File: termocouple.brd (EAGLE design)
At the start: 69.8 x 100 mm, 19 parts, among them IC1 MAX6675, IC2 MAX6675, U2 TC1262_VDB, X2 1751248, X3 1751248

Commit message: updated brd
finished routing PCB
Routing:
- net N$12: track 0.00 -> 94.5 mm, vias 0 -> 1
- net N$11: track 0.00 -> 88.4 mm, vias 0 -> 1
- net N$9: track 0.00 -> 73.2 mm, vias 0 -> 1
- net N$23: track 0.00 -> 65.2 mm, vias 0 -> 1
- net N$22: track 0.00 -> 64.0 mm, vias 0 -> 1
- net +3V3: track 194.9 -> 181.8 mm
- net VJ: track 6.70 -> 8.97 mm
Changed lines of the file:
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@@
 <wire x1="10.29" y1="41.91" x2="10.29" y2="44.32" width="0.8128" layer="1"/>
 <wire x1="10.29" y1="44.32" x2="8.89" y2="45.72" width="0.8128" layer="1"/>
-<wire x1="8.89" y1="45.72" x2="6.985" y2="45.72" width="0.8128" layer="1"/>
-<wire x1="6.985" y1="45.72" x2="5.08" y2="45.72" width="0.8128" layer="1"/>
+<wire x1="8.89" y1="45.72" x2="5.08" y2="45.72" width="0.8128" layer="1"/>
 <wire x1="5.08" y1="45.72" x2="3.81" y2="46.99" width="0.8128" layer="1"/>
-<wire x1="3.81" y1="46.99" x2="3.81" y2="80.01" width="0.8128" layer="1"/>
+<wire x1="3.81" y1="46.99" x2="3.81" y2="60.96" width="0.8128" layer="1"/>
+<wire x1="3.81" y1="60.96" x2="3.81" y2="80.01" width="0.8128" layer="1"/>
 <wire x1="3.81" y1="80.01" x2="11.43" y2="87.63" width="0.8128" layer="1"/>
 <wire x1="11.43" y1="87.63" x2="20.32" y2="87.63" width="0.8128" layer="1"/>
-<wire x1="55.88" y1="60.96" x2="8.255" y2="60.96" width="0.6096" layer="16"/>
-<wire x1="8.255" y1="60.96" x2="6.985" y2="59.69" width="0.6096" layer="16"/>
-<wire x1="6.985" y1="59.69" x2="6.985" y2="45.72" width="0.6096" layer="16"/>
-<via x="6.985" y="45.72" extent="1-16" drill="0.6" shape="square"/>
+<wire x1="54.61" y1="60.96" x2="8.255" y2="60.96" width="0.6096" layer="16"/>
 <wire x1="60.325" y1="31.2166" x2="60.325" y2="34.29" width="0.6096" layer="1"/>
 <wire x1="60.325" y1="34.29" x2="43.815" y2="34.29" width="0.6096" layer="1"/>
@@
 <wire x1="64.77" y1="34.29" x2="60.325" y2="34.29" width="0.4064" layer="16"/>
 <via x="60.325" y="34.29" extent="1-16" drill="0.6" shape="square"/>
-<wire x1="55.88" y1="60.96" x2="55.88" y2="57.785" width="0.4064" layer="16"/>
-<wire x1="55.88" y1="57.785" x2="54.61" y2="56.515" width="0.4064" layer="16"/>
-<wire x1="54.61" y1="56.515" x2="54.61" y2="48.26" width="0.4064" layer="16"/>
+<wire x1="54.61" y1="60.96" x2="54.61" y2="48.26" width="0.6096" layer="16"/>
+<via x="8.255" y="60.96" extent="1-16" drill="0.6" shape="square"/>
+<wire x1="8.255" y1="60.96" x2="3.81" y2="60.96" width="0.6096" layer="1"/>
 </signal>
 <signal name="GND">
@@
 <contactref element="SV1" pad="2"/>
 <contactref element="SV1" pad="6"/>
+<via x="22.86" y="8.255" extent="1-16" drill="0.6" shape="square"/>
+<via x="32.385" y="57.15" extent="1-16" drill="0.6" shape="square"/>
+<via x="26.67" y="68.58" extent="1-16" drill="0.6" shape="square"/>
+<via x="32.385" y="69.215" extent="1-16" drill="0.6" shape="square"/>
+<via x="32.385" y="79.375" extent="1-16" drill="0.6" shape="square"/>
+<via x="26.67" y="78.105" extent="1-16" drill="0.6" shape="square"/>
+<via x="65.405" y="51.435" extent="1-16" drill="0.6" shape="square"/>
+<via x="39.37" y="48.26" extent="1-16" drill="0.6" shape="square"/>
+<via x="39.37" y="48.26" extent="1-16" drill="0.6" shape="square"/>
+<via x="20.955" y="41.91" extent="1-16" drill="0.6" shape="square"/>
+<via x="6.985" y="56.515" extent="1-16" drill="0.6" shape="square"/>
 </signal>
 <signal name="N$4">
@@
 <wire x1="5.89289375" y1="13.77779375" x2="5.42" y2="14.41279375" width="0.8128" layer="1"/>
 <wire x1="5.42" y1="14.41279375" x2="5.42" y2="20.32" width="0.8128" layer="1"/>
-<wire x1="5.89289375" y1="13.77779375" x2="8.09625" y2="13.795" width="0" layer="19" extent="1-1"/>
+<wire x1="6.35" y1="13.97" x2="7.62" y2="13.97" width="0.254" layer="1"/>
+<wire x1="7.62" y1="13.97" x2="8.09625" y2="13.795" width="0.254" layer="1"/>
+<wire x1="6.35" y1="13.97" x2="5.89289375" y2="13.77779375" width="0.254" layer="1"/>
 </signal>
 <signal name="N$18">
@@
 <contactref element="U$1" pad="D6"/>
 <contactref element="X1" pad="5"/>
-<wire x1="30.48" y1="19.05" x2="30.48" y2="87.63" width="0" layer="19" extent="1-1"/>
+<wire x1="30.48" y1="19.05" x2="27.94" y2="19.05" width="0.4064" layer="16"/>
+<wire x1="27.94" y1="19.05" x2="26.67" y2="20.32" width="0.4064" layer="16"/>
+<wire x1="26.67" y1="20.32" x2="26.67" y2="40.005" width="0.4064" layer="16"/>
+<wire x1="26.67" y1="40.005" x2="29.21" y2="42.545" width="0.4064" layer="16"/>
+<wire x1="29.21" y1="42.545" x2="29.21" y2="58.42" width="0.4064" layer="16"/>
+<via x="29.21" y="58.42" extent="1-16" drill="0.6" shape="square"/>
+<wire x1="29.21" y1="58.42" x2="29.21" y2="81.915" width="0.4064" layer="1"/>
+<wire x1="29.21" y1="81.915" x2="30.48" y2="83.185" width="0.4064" layer="1"/>
+<wire x1="30.48" y1="83.185" x2="30.48" y2="87.63" width="0.4064" layer="1"/>
 </signal>
 <signal name="N$10">
@@
 <contactref element="U$1" pad="D4"/>
 <contactref element="X1" pad="7"/>
-<wire x1="30.48" y1="13.97" x2="35.56" y2="87.63" width="0" layer="19" extent="1-1"/>
+<wire x1="30.48" y1="13.97" x2="25.4" y2="13.97" width="0.4064" layer="16"/>
+<wire x1="25.4" y1="13.97" x2="24.13" y2="15.24" width="0.4064" layer="16"/>
+<wire x1="24.13" y1="15.24" x2="24.13" y2="39.37" width="0.4064" layer="16"/>
+<wire x1="24.13" y1="39.37" x2="27.94" y2="43.18" width="0.4064" layer="16"/>
+<wire x1="27.94" y1="43.18" x2="27.94" y2="52.07" width="0.4064" layer="16"/>
+<wire x1="27.94" y1="52.07" x2="26.67" y2="53.34" width="0.4064" layer="16"/>
+<via x="26.67" y="53.34" extent="1-16" drill="0.6" shape="square"/>
+<wire x1="26.67" y1="53.34" x2="32.385" y2="53.34" width="0.4064" layer="1"/>
+<wire x1="32.385" y1="53.34" x2="35.56" y2="56.515" width="0.4064" layer="1"/>
+<wire x1="35.56" y1="56.515" x2="35.56" y2="87.63" width="0.4064" layer="1"/>
 </signal>
 <signal name="N$12">
 <contactref element="U$1" pad="D3"/>
 <contactref element="X1" pad="8"/>
-<wire x1="30.48" y1="11.43" x2="38.1" y2="87.63" width="0" layer="19" extent="1-1"/>
+<wire x1="30.48" y1="11.43" x2="22.86" y2="11.43" width="0.4064" layer="16"/>
+<wire x1="22.86" y1="11.43" x2="22.225" y2="12.065" width="0.4064" layer="16"/>
+<wire x1="22.225" y1="12.065" x2="22.225" y2="39.37" width="0.4064" layer="16"/>
+<wire x1="22.225" y1="39.37" x2="26.67" y2="43.815" width="0.4064" layer="16"/>
+<wire x1="26.67" y1="43.815" x2="26.67" y2="48.26" width="0.4064" layer="16"/>
+<wire x1="26.67" y1="48.26" x2="26.035" y2="48.895" width="0.4064" layer="16"/>
+<via x="26.035" y="48.895" extent="1-16" drill="0.6" shape="square"/>
+<wire x1="26.035" y1="48.895" x2="31.75" y2="48.895" width="0.4064" layer="1"/>
+<wire x1="31.75" y1="48.895" x2="38.1" y2="55.245" width="0.4064" layer="1"/>
+<wire x1="38.1" y1="55.245" x2="38.1" y2="87.63" width="0.4064" layer="1"/>
 </signal>
 <signal name="N$22">
 <contactref element="U$1" pad="D0"/>
 <contactref element="X6" pad="3"/>
-<wire x1="15.24" y1="11.43" x2="15.875" y2="67.945" width="0" layer="19" extent="1-1"/>
+<wire x1="15.24" y1="11.43" x2="17.78" y2="11.43" width="0.4064" layer="16"/>
+<wire x1="17.78" y1="11.43" x2="17.78" y2="53.34" width="0.4064" layer="16"/>
+<via x="17.78" y="53.34" extent="1-16" drill="0.6" shape="square"/>
+<wire x1="17.78" y1="53.34" x2="20.32" y2="53.34" width="0.4064" layer="1"/>
+<wire x1="20.32" y1="53.34" x2="20.955" y2="53.975" width="0.4064" layer="1"/>
+<wire x1="20.955" y1="53.975" x2="20.955" y2="62.865" width="0.4064" layer="1"/>
+<wire x1="20.955" y1="62.865" x2="15.875" y2="67.945" width="0.4064" layer="1"/>
 </signal>
 <signal name="N$23">
 <contactref element="U$1" pad="D1"/>
 <contactref element="X6" pad="2"/>
-<wire x1="15.24" y1="8.89" x2="13.335" y2="67.945" width="0" layer="19" extent="1-1"/>
+<wire x1="15.24" y1="8.89" x2="19.05" y2="8.89" width="0.4064" layer="16"/>
+<wire x1="19.05" y1="8.89" x2="19.05" y2="57.785" width="0.4064" layer="16"/>
+<via x="19.05" y="57.785" extent="1-16" drill="0.6" shape="square"/>
+<wire x1="19.05" y1="57.785" x2="19.05" y2="58.42" width="0.4064" layer="1"/>
+<wire x1="19.05" y1="58.42" x2="13.335" y2="64.135" width="0.4064" layer="1"/>
+<wire x1="13.335" y1="64.135" x2="13.335" y2="67.945" width="0.4064" layer="1"/>
 </signal>
 <signal name="N$7">

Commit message: pdf version of schematics
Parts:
- IC1, IC2: value MAX6675 -> MAX31855
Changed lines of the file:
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@@
 <elements>
 <element name="U$1" library="mine" package="EMPHYREAN" value="EPHYREAN" x="22.86" y="26.67"/>
-<element name="IC1" library="adafruit" package="SO08" value="MAX6675" x="41.91" y="34.29"/>
-<element name="IC2" library="adafruit" package="SO08" value="MAX6675" x="58.42" y="34.29"/>
+<element name="IC1" library="adafruit" package="SO08" value="MAX31855" x="41.91" y="34.29"/>
+<element name="IC2" library="adafruit" package="SO08" value="MAX31855" x="58.42" y="34.29"/>
 <element name="X1" library="con-phoenix-254" package="10POL254" value="" x="31.75" y="87.63">
 <attribute name="OC_NEWARK" value="unknown" x="58.42" y="24.13" size="1.778" layer="27" display="off"/>

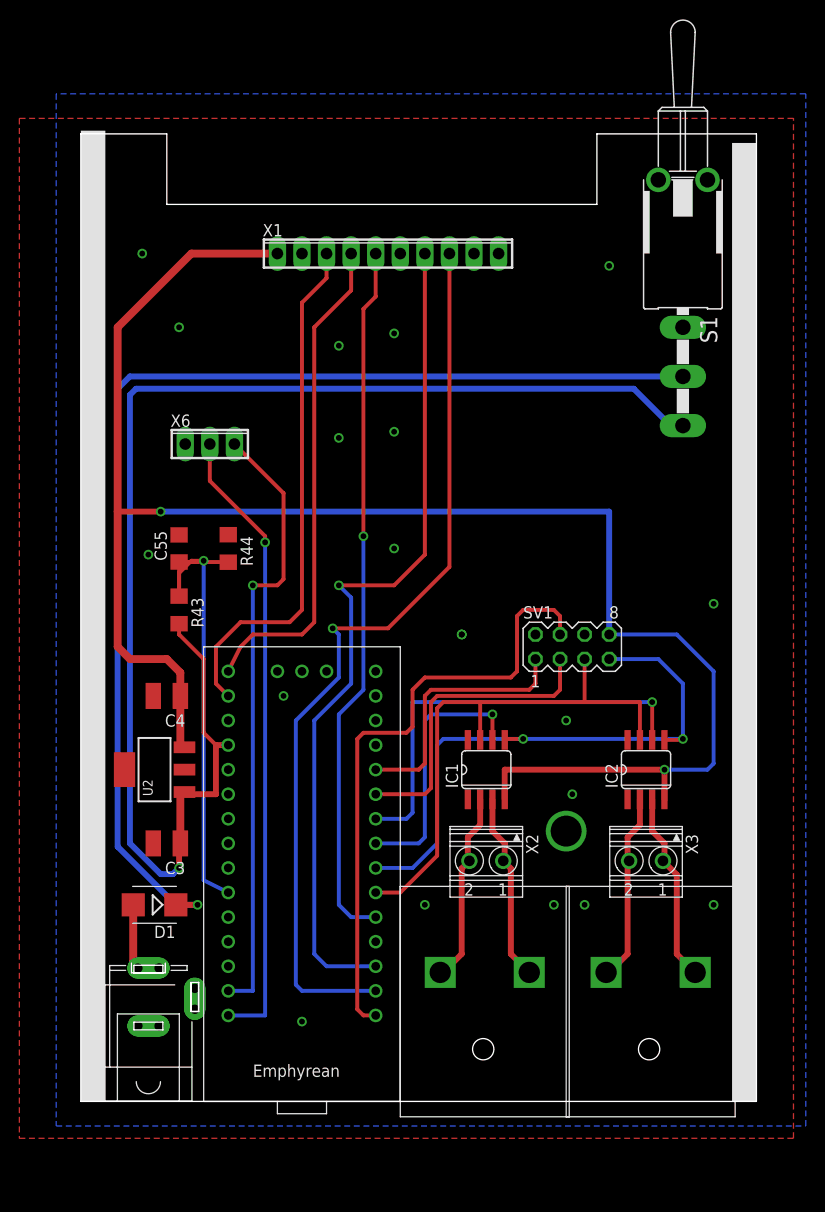
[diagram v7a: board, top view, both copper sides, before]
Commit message: pcb fix
Fix PCB's to make it possible to build the boards without rework
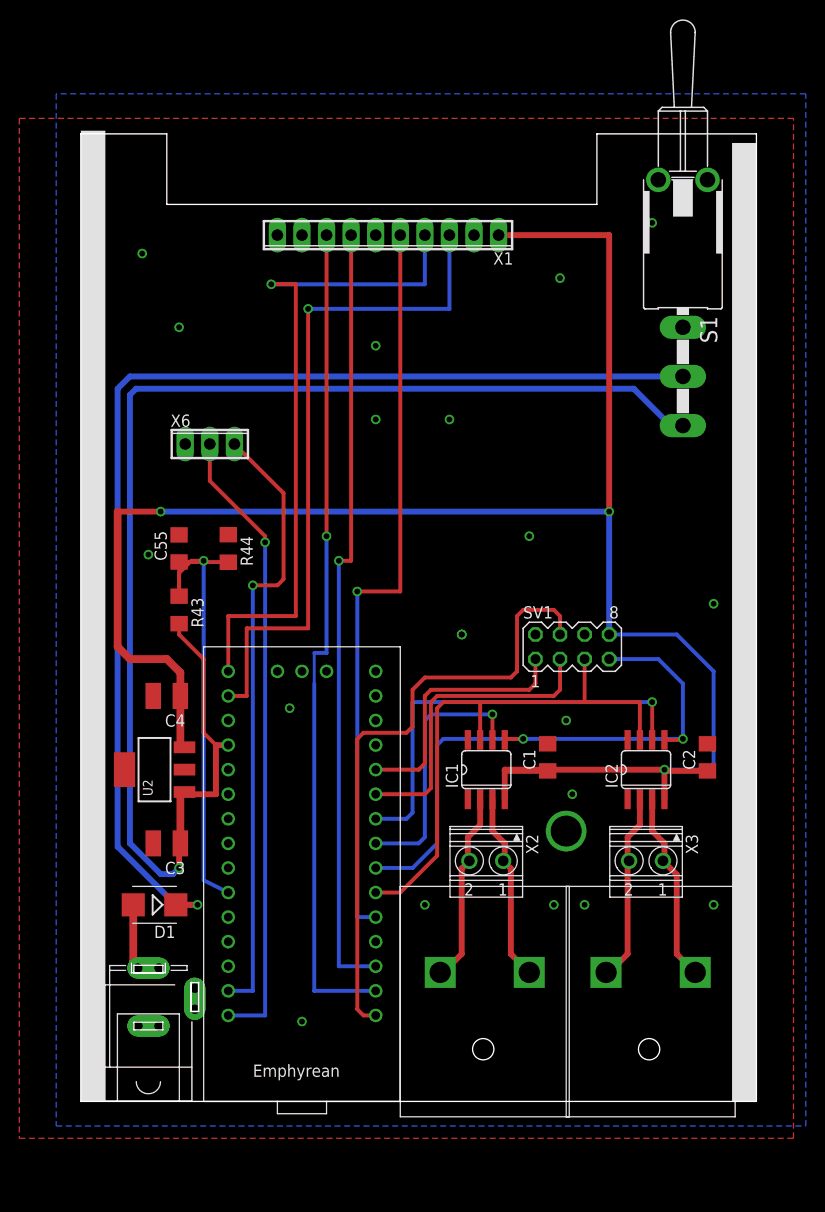
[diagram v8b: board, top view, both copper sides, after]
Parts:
- added C1, C2: 100n, rcl:C1206
- moved X1 1.91 mm to (31.8, 89.5), turned to 180 degrees
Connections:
- net +3V3: now also C1.1, C2.1
- net GND: now also C1.2, C2.2
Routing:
- net N$8: track 51.2 -> 70.5 mm, vias 0 -> 1
- net N$5: track 54.0 -> 70.5 mm, vias 0 -> 1
- net +3V3: track 181.8 -> 192.1 mm, vias 2 -> 3
- net N$12: track 94.5 -> 85.7 mm
- net N$11: track 88.4 -> 80.6 mm
- net N$9: track 73.2 -> 76.8 mm
